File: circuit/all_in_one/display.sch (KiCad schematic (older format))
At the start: 0 parts

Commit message: [IN-14]Add IN-14 circuit
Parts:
- added U10, U11, U12, U13, U14, U15, U16, U17: IN-14, symbol IN-14
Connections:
- new net: U10.10 (Cathode_8), U12.10 (Cathode_8), U14.10 (Cathode_8), U16.10 (Cathode_8)
- new net: U10.11 (Cathode_9), U12.11 (Cathode_9), U14.11 (Cathode_9), U16.11 (Cathode_9)
- new net: U10.12 (Cathode_0), U12.12 (Cathode_0), U14.12 (Cathode_0), U16.12 (Cathode_0)
- new net: U10.13 (Cathode_Camma_Right), U11.13 (Cathode_Camma_Right), U12.13 (Cathode_Camma_Right), U13.13 (Cathode_Camma_Right), U14.13 (Cathode_Camma_Right), U15.13 (Cathode_Camma_Right), U16.13 (Cathode_Camma_Right), U17.13 (Cathode_Camma_Right)
- new net: U10.2 (Cathode_Comma_Left), U11.2 (Cathode_Comma_Left), U12.2 (Cathode_Comma_Left), U13.2 (Cathode_Comma_Left), U14.2 (Cathode_Comma_Left), U15.2 (Cathode_Comma_Left), U16.2 (Cathode_Comma_Left), U17.2 (Cathode_Comma_Left)
- new net: U10.3 (Cathode_1), U11.3 (Cathode_1), U12.3 (Cathode_1), U13.3 (Cathode_1), U14.3 (Cathode_1), U15.3 (Cathode_1), U16.3 (Cathode_1), U17.3 (Cathode_1)
- new net: U10.4 (Cathode_2), U11.4 (Cathode_2), U12.4 (Cathode_2), U13.4 (Cathode_2), U14.4 (Cathode_2), U15.4 (Cathode_2), U16.4 (Cathode_2), U17.4 (Cathode_2)
- new net: U10.5 (Cathode_3), U11.5 (Cathode_3), U12.5 (Cathode_3), U13.5 (Cathode_3), U14.5 (Cathode_3), U15.5 (Cathode_3), U16.5 (Cathode_3), U17.5 (Cathode_3)
- new net: U10.6 (Cathode_4), U11.6 (Cathode_4), U12.6 (Cathode_4), U13.6 (Cathode_4), U14.6 (Cathode_4), U15.6 (Cathode_4), U16.6 (Cathode_4), U17.6 (Cathode_4)
- new net: U10.7 (Cathode_5), U12.7 (Cathode_5), U14.7 (Cathode_5), U16.7 (Cathode_5)
- new net: U10.8 (Cathode_6), U12.8 (Cathode_6), U14.8 (Cathode_6), U16.8 (Cathode_6)
- new net: U10.9 (Cathode_7), U12.9 (Cathode_7), U14.9 (Cathode_7), U16.9 (Cathode_7)
- new net: U11.10 (Cathode_8), U13.10 (Cathode_8), U15.10 (Cathode_8), U17.10 (Cathode_8)
- new net: U11.11 (Cathode_9), U13.11 (Cathode_9), U15.11 (Cathode_9), U17.11 (Cathode_9)
- new net: U11.12 (Cathode_0), U13.12 (Cathode_0), U15.12 (Cathode_0), U17.12 (Cathode_0)
- new net: U11.7 (Cathode_5), U13.7 (Cathode_5), U15.7 (Cathode_5), U17.7 (Cathode_5)
- new net: U11.8 (Cathode_6), U13.8 (Cathode_6), U15.8 (Cathode_6), U17.8 (Cathode_6)
- new net: U11.9 (Cathode_7), U13.9 (Cathode_7), U15.9 (Cathode_7), U17.9 (Cathode_7)

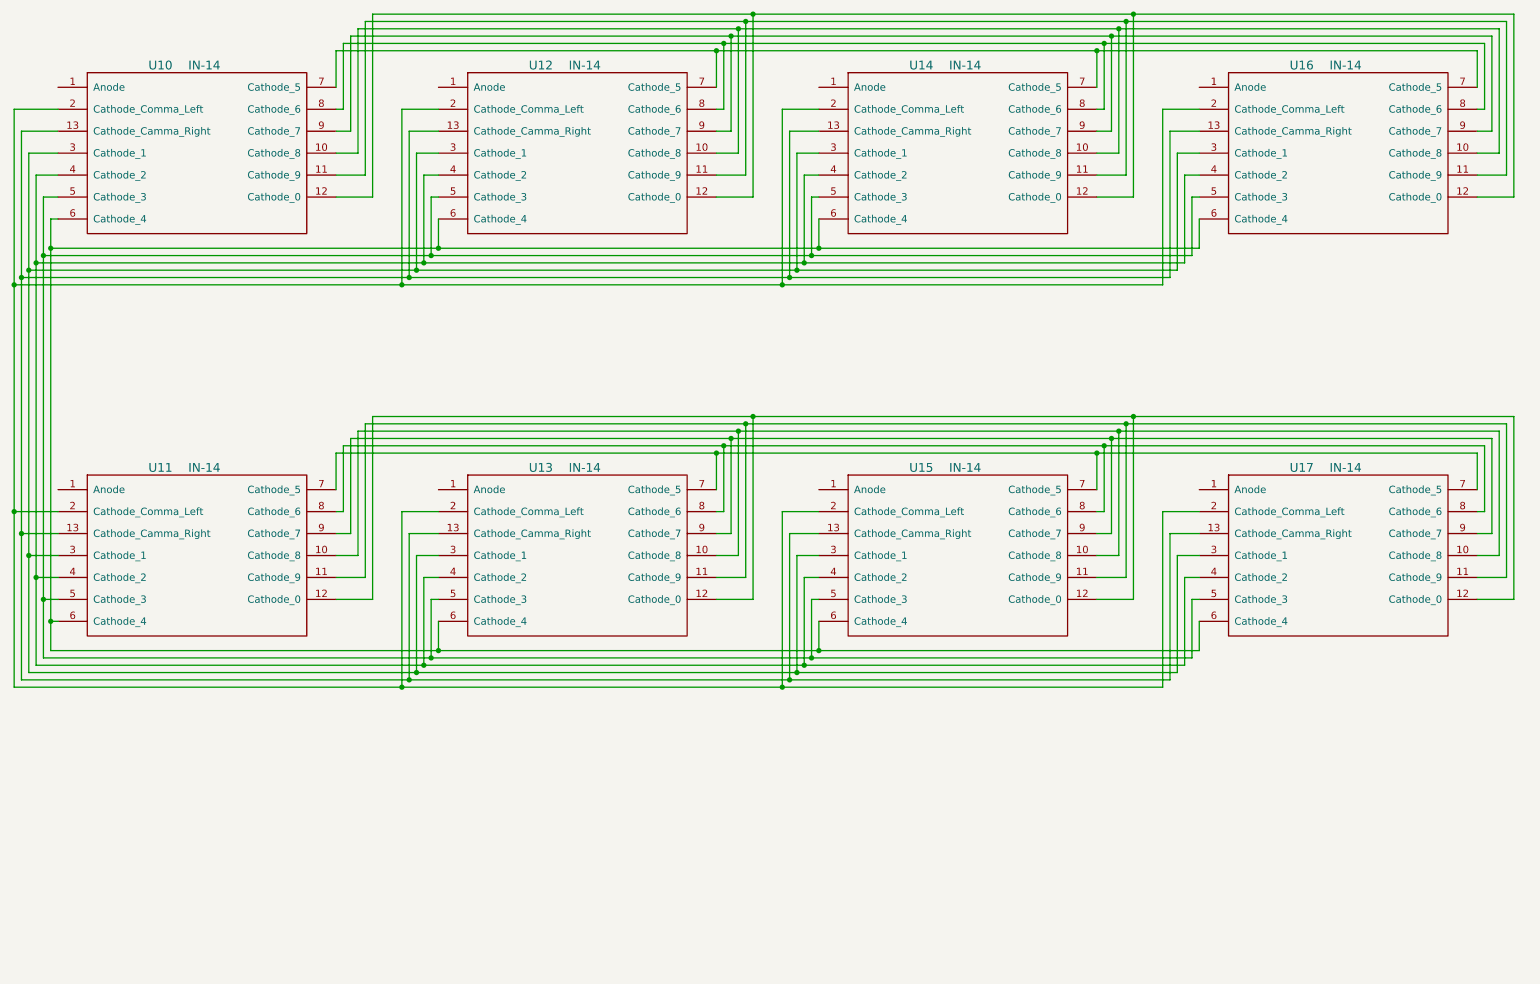
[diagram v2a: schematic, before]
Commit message: [All in one]Finish the tube display circuit
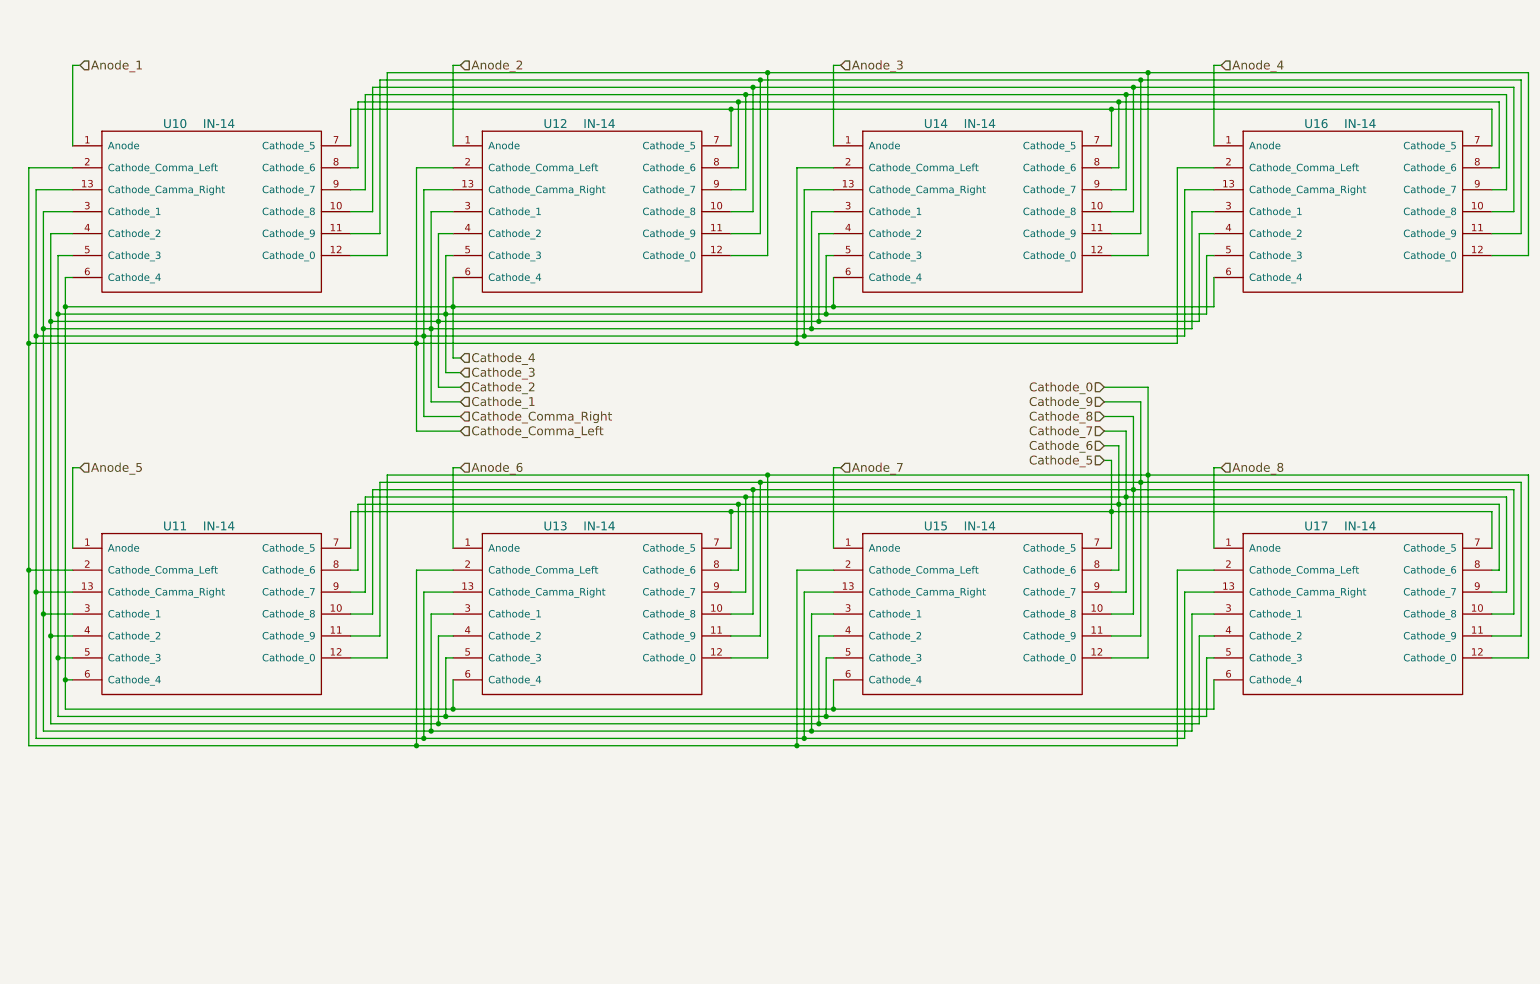
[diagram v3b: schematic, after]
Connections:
- net Anode_1: now reaches U10.1 (Anode)
- net Cathode_Comma_Right: now reaches U10.13 (Cathode_Camma_Right), U11.13 (Cathode_Camma_Right), U12.13 (Cathode_Camma_Right), U13.13 (Cathode_Camma_Right), U14.13 (Cathode_Camma_Right), U15.13 (Cathode_Camma_Right), U16.13 (Cathode_Camma_Right), U17.13 (Cathode_Camma_Right)
- net Cathode_Comma_Left: now reaches U10.2 (Cathode_Comma_Left), U11.2 (Cathode_Comma_Left), U12.2 (Cathode_Comma_Left), U13.2 (Cathode_Comma_Left), U14.2 (Cathode_Comma_Left), U15.2 (Cathode_Comma_Left), U16.2 (Cathode_Comma_Left), U17.2 (Cathode_Comma_Left)
- net Cathode_1: now reaches U10.3 (Cathode_1), U11.3 (Cathode_1), U12.3 (Cathode_1), U13.3 (Cathode_1), U14.3 (Cathode_1), U15.3 (Cathode_1), U16.3 (Cathode_1), U17.3 (Cathode_1)
- net Cathode_2: now reaches U10.4 (Cathode_2), U11.4 (Cathode_2), U12.4 (Cathode_2), U13.4 (Cathode_2), U14.4 (Cathode_2), U15.4 (Cathode_2), U16.4 (Cathode_2), U17.4 (Cathode_2)
- net Cathode_3: now reaches U10.5 (Cathode_3), U11.5 (Cathode_3), U12.5 (Cathode_3), U13.5 (Cathode_3), U14.5 (Cathode_3), U15.5 (Cathode_3), U16.5 (Cathode_3), U17.5 (Cathode_3)
- net Cathode_4: now reaches U10.6 (Cathode_4), U11.6 (Cathode_4), U12.6 (Cathode_4), U13.6 (Cathode_4), U14.6 (Cathode_4), U15.6 (Cathode_4), U16.6 (Cathode_4), U17.6 (Cathode_4)
- net Anode_2: now reaches U12.1 (Anode)
- net Anode_3: now reaches U14.1 (Anode)
- net Anode_4: now reaches U16.1 (Anode)
- net Anode_5: now reaches U11.1 (Anode)
- net Cathode_8: now reaches U11.10 (Cathode_8), U13.10 (Cathode_8), U15.10 (Cathode_8), U17.10 (Cathode_8)
- net Cathode_9: now reaches U11.11 (Cathode_9), U13.11 (Cathode_9), U15.11 (Cathode_9), U17.11 (Cathode_9)
- net Cathode_0: now reaches U11.12 (Cathode_0), U13.12 (Cathode_0), U15.12 (Cathode_0), U17.12 (Cathode_0)
- net Cathode_5: now reaches U11.7 (Cathode_5), U13.7 (Cathode_5), U15.7 (Cathode_5), U17.7 (Cathode_5)
- net Cathode_6: now reaches U11.8 (Cathode_6), U13.8 (Cathode_6), U15.8 (Cathode_6), U17.8 (Cathode_6)
- net Cathode_7: now reaches U11.9 (Cathode_7), U13.9 (Cathode_7), U15.9 (Cathode_7), U17.9 (Cathode_7)
- net Anode_6: now reaches U13.1 (Anode)
- net Anode_7: now reaches U15.1 (Anode)
- net Anode_8: now reaches U17.1 (Anode)
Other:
- moved on the sheet: U10, U11, U12, U13, U14, U15, U16, U17

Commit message: [All in one circuit]Import IN-14 library
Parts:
- U10, U11, U12, U13, U14, U15, U16, U17: footprint (none) -> IN-14:IN-14
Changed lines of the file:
@@
 F 0 "U10" H 1700 2900 60  0000 C CNN
 F 1 "IN-14" H 2000 2900 60  0000 C CNN
-F 2 "" H 1700 2900 60  0000 C CNN
+F 2 "IN-14:IN-14" H 1700 2900 60  0001 C CNN
 F 3 "" H 1700 2900 60  0000 C CNN
 	1    1950 2250
@@
 F 0 "U12" H 4300 2900 60  0000 C CNN
 F 1 "IN-14" H 4600 2900 60  0000 C CNN
-F 2 "" H 4300 2900 60  0000 C CNN
+F 2 "IN-14:IN-14" H 4300 2900 60  0001 C CNN
 F 3 "" H 4300 2900 60  0000 C CNN
 	1    4550 2250
@@
 F 0 "U14" H 6900 2900 60  0000 C CNN
 F 1 "IN-14" H 7200 2900 60  0000 C CNN
-F 2 "" H 6900 2900 60  0000 C CNN
+F 2 "IN-14:IN-14" H 6900 2900 60  0001 C CNN
 F 3 "" H 6900 2900 60  0000 C CNN
 	1    7150 2250
@@
 F 0 "U16" H 9500 2900 60  0000 C CNN
 F 1 "IN-14" H 9800 2900 60  0000 C CNN
-F 2 "" H 9500 2900 60  0000 C CNN
+F 2 "IN-14:IN-14" H 9500 2900 60  0001 C CNN
 F 3 "" H 9500 2900 60  0000 C CNN
 	1    9750 2250
@@
 F 0 "U11" H 1700 5650 60  0000 C CNN
 F 1 "IN-14" H 2000 5650 60  0000 C CNN
-F 2 "" H 1700 5650 60  0000 C CNN
+F 2 "IN-14:IN-14" H 1700 5650 60  0001 C CNN
 F 3 "" H 1700 5650 60  0000 C CNN
 	1    1950 5000
@@
 F 0 "U13" H 4300 5650 60  0000 C CNN
 F 1 "IN-14" H 4600 5650 60  0000 C CNN
-F 2 "" H 4300 5650 60  0000 C CNN
+F 2 "IN-14:IN-14" H 4300 5650 60  0001 C CNN
 F 3 "" H 4300 5650 60  0000 C CNN
 	1    4550 5000
@@
 F 0 "U15" H 6900 5650 60  0000 C CNN
 F 1 "IN-14" H 7200 5650 60  0000 C CNN
-F 2 "" H 6900 5650 60  0000 C CNN
+F 2 "IN-14:IN-14" H 6900 5650 60  0001 C CNN
 F 3 "" H 6900 5650 60  0000 C CNN
 	1    7150 5000
@@
 F 0 "U17" H 9500 5650 60  0000 C CNN
 F 1 "IN-14" H 9800 5650 60  0000 C CNN
-F 2 "" H 9500 5650 60  0000 C CNN
+F 2 "IN-14:IN-14" H 9500 5650 60  0001 C CNN
 F 3 "" H 9500 5650 60  0000 C CNN
 	1    9750 5000
